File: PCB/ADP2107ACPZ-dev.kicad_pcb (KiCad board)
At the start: 2 copper layers, 17 parts, among them P1 CONN_01X02, P2 CONN_01X02, U1 ADP2107

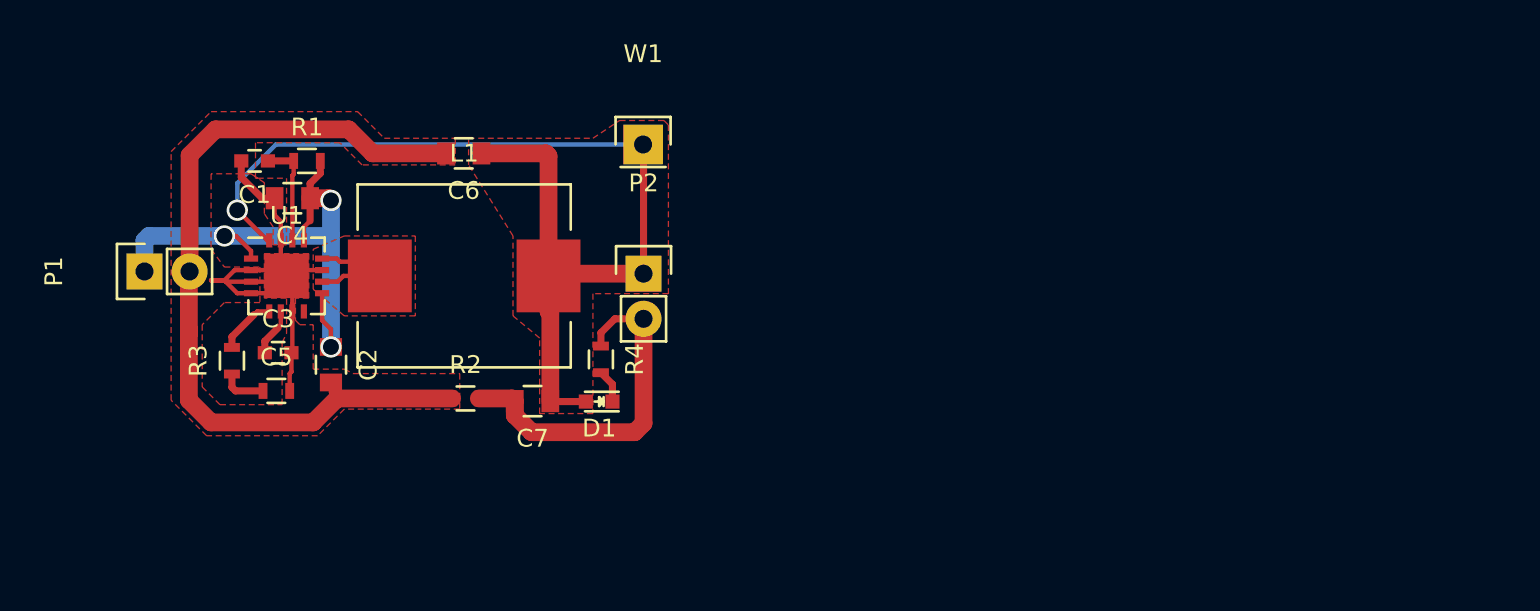
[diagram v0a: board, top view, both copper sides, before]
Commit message: Datenblätter der Sende- und Verstärkerchips dazugefügt
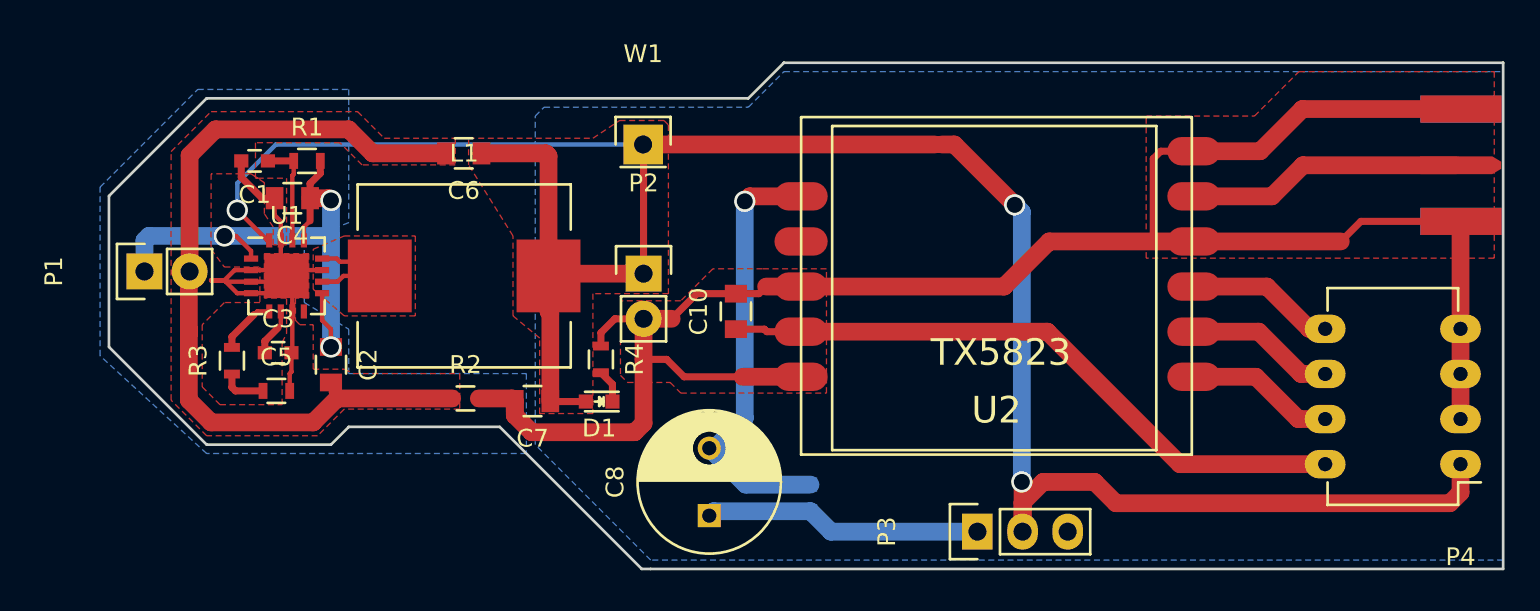
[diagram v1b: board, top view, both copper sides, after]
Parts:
- added C10: 10u, Capacitors_SMD:C_0805, F.Cu at (201.3, 108.0)
- added C8: 470u, Capacitors_ThroughHole:C_Radial_D8_L13_P3.8, F.Cu at (199.8, 119.5)
- added C9: 100n, Capacitors_SMD:C_0603, B.Cu at (205.5, 118.5)
- added P3: CONN_01X03, Pin_Headers:Pin_Header_Straight_1x03, F.Cu at (214.9, 120.4)
- added P4: CONN_02X04, Housings_DIP:DIP-8_W7.62mm_LongPads, F.Cu at (242.1, 116.6)
- added SMA_E1: SMA_EDGE, library_toni:SMA_EDGE, F.Cu at (251.0, 98.5)
- added U2: TX5823, library_toni:TX5823, F.Cu at (216.4, 106.6)
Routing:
- net GND: track 22.3 -> 122.2 mm
- net +3.3VP: track 60.2 -> 129.8 mm, vias 1 -> 3
- net Net-(C10-Pad1): track 0.00 -> 36.3 mm
- net Net-(C8-Pad2): track 0.00 -> 24.7 mm, vias 0 -> 1
- net Net-(SMA_E1-Pad1): track 0.00 -> 17.8 mm
- net Net-(C8-Pad1): track 0.00 -> 15.9 mm
- net Net-(P4-Pad8): track 0.00 -> 8.38 mm
- net Net-(P4-Pad6): track 0.00 -> 8.38 mm
- net Net-(P4-Pad4): track 0.00 -> 8.38 mm
- added copper zone on B.Cu, net GND
- added copper zone on F.Cu, net GND
- added copper zone on B.Cu, net GNDPWR
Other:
- board outline added: 78.5 x 28.5 mm
